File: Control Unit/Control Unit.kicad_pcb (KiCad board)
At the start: 2 copper layers, 100 x 76.5 mm, 17 parts, among them J1 PWR_IN, J2 LM2596S, J3 ST7789, J4 DHT20, J5 RTC, J6 RPM_IN, J7 Page flip, SW1 SW_DPST_x2, U1 ESP32-DEVKIT-V1, U2 PC817

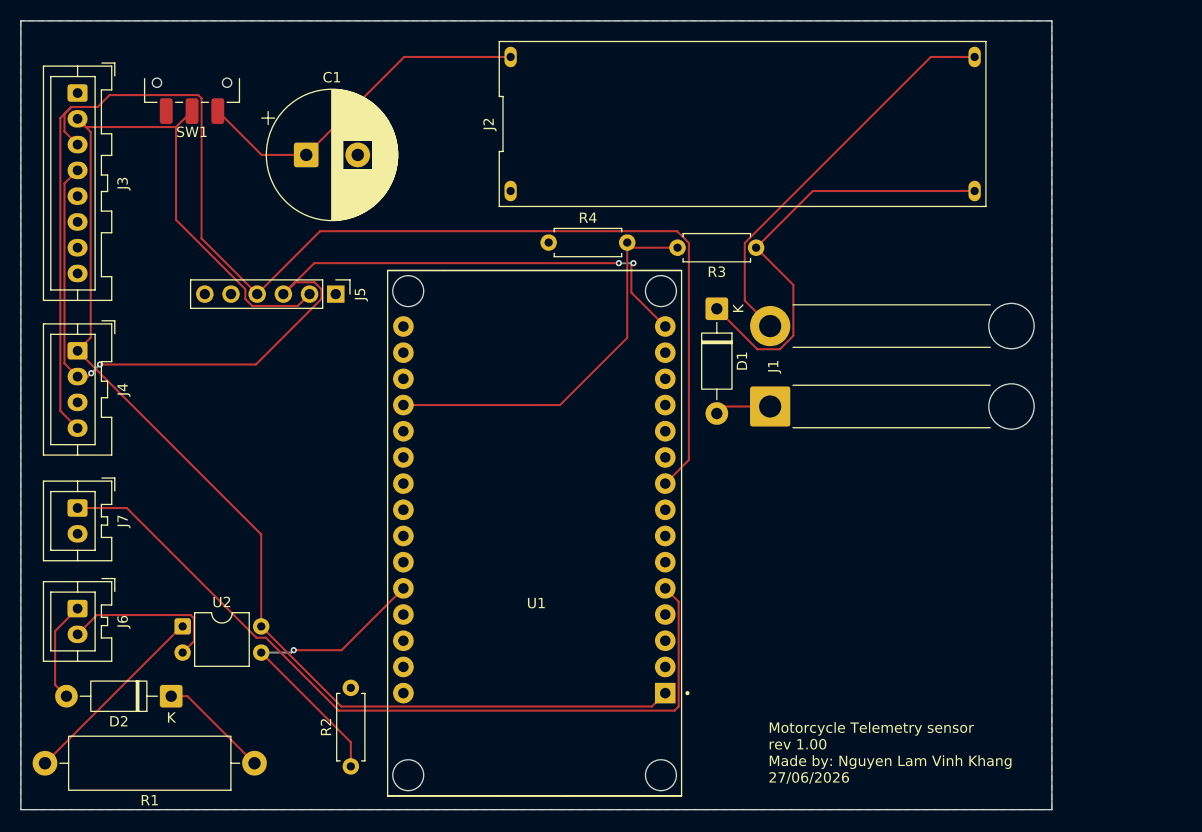
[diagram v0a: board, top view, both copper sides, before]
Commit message: rev 1.1: added relay to use power directly from battery
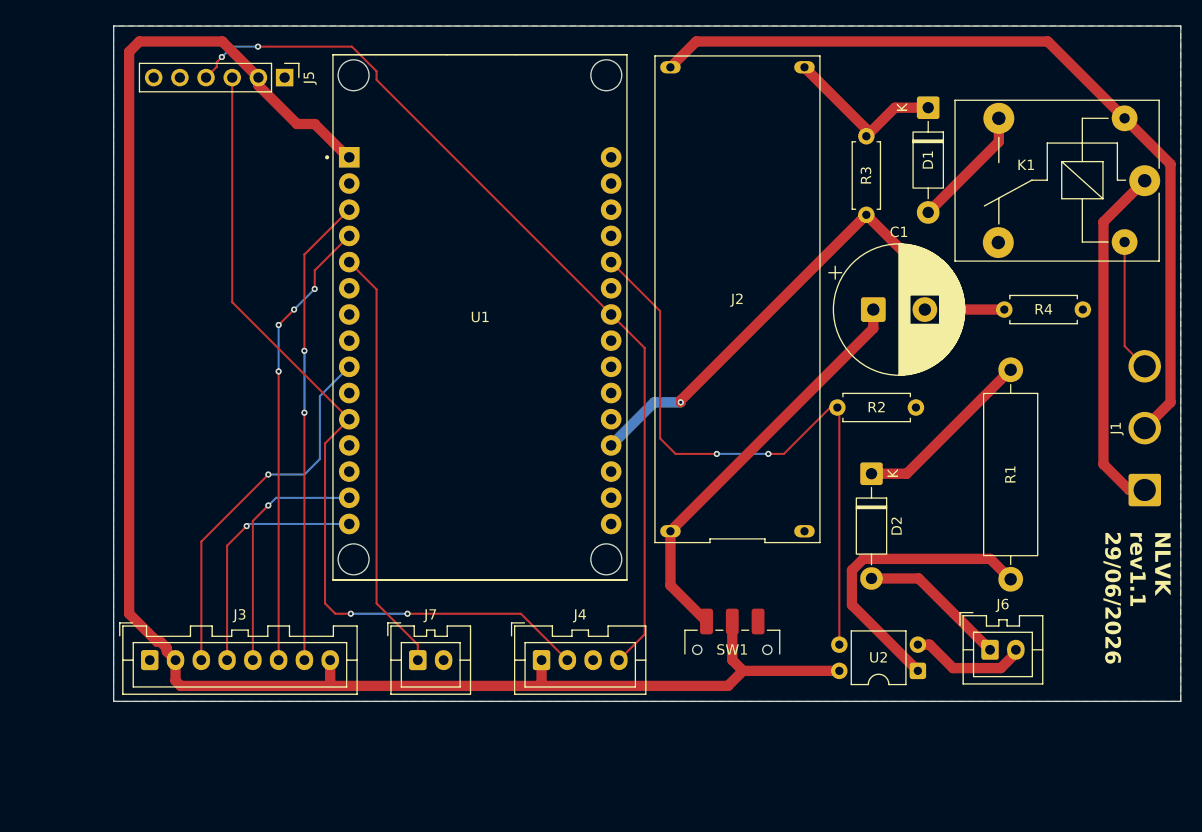
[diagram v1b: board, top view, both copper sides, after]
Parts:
- added K1: Relay_SPDT, Relay_THT:Relay_SPDT_SANYOU_SRD_Series_Form_C, F.Cu at (201.5, 95.0)
- J1: value PWR_IN -> Conn_01x03_Pin; footprint Connector_Wire:SolderWire-1.5sqmm_1x02_P7.8mm_D1.7mm_OD3.9mm_Relief -> Connector_Wire:SolderWire-1.5sqmm_1x03_P6mm_D1.7mm_OD3mm
- moved J6 88.6 mm to (186.5, 140.5), turned to 0 degrees
- moved R1 82.7 mm to (188.5, 113.3), turned to -90 degrees
- moved SW1 76.0 mm to (161.5, 140.5), turned to 0 degrees
- moved U2 71.4 mm to (179.5, 142.5), turned to 180 degrees
- moved D2 71.3 mm to (175.0, 123.4), turned to -90 degrees
- moved R2 58.6 mm to (171.7, 117.0), turned to 0 degrees
- moved C1 57.0 mm to (175.2, 107.5)
- moved J3 55.4 mm to (105.0, 141.5), turned to 0 degrees
- moved J4 54.1 mm to (143.0, 141.5), turned to 0 degrees
- moved R4 52.2 mm to (195.5, 107.5), turned to 180 degrees
- moved J1 37.2 mm to (201.5, 125.0)
- moved J7 36.1 mm to (131.0, 141.5), turned to 0 degrees
- moved D1 28.3 mm to (180.5, 87.9)
- moved U1 21.6 mm to (137.1, 108.2), turned to 0 degrees
- moved J5 21.6 mm to (118.1, 85.0)
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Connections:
- J1 pad 1: /12V_PWR_BATT -> /12V_PWR_Relay
- J3 pad 5: unconnected-(J3-RES-Pad5) -> Net-(J3-RES)
- J3 pad 6: unconnected-(J3-DC-Pad6) -> Net-(J3-DC)
- J3 pad 7: unconnected-(J3-CS-Pad7) -> Net-(J3-CS)
- J3 pad 8: unconnected-(J3-Pin_8-Pad8) -> /3.3V_PWR
- J4 pad 2: Net-(J3-SDA) -> Net-(J4-SDA)
- J4 pad 4: Net-(J3-SCL) -> Net-(J4-SCL)
- J5 pad 3: Net-(J3-SDA) -> Net-(J4-SDA)
- J5 pad 4: Net-(J3-SCL) -> Net-(J4-SCL)
- U1 pad 11: unconnected-(U1-D21-Pad11) -> Net-(J4-SDA)
- U1 pad 14: unconnected-(U1-D22-Pad14) -> Net-(J3-RES)
- U1 pad 24: unconnected-(U1-D26-Pad24) -> Net-(J4-SCL)
- U1 pad 3: unconnected-(U1-D15-Pad3) -> Net-(J3-CS)
- U1 pad 4: unconnected-(U1-D2-Pad4) -> Net-(J3-DC)
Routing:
- net Net-(J3-SCL): track 140.4 -> 36.4 mm, vias 0 -> 1
- net Net-(J4-SCL): track 0.00 -> 88.0 mm, vias 0 -> 2
- net Net-(J4-SDA): track 0.00 -> 82.5 mm, vias 0 -> 2
- net Net-(J3-SDA): track 96.0 -> 23.8 mm, vias 4 -> 1
- net Net-(J3-CS): track 0.00 -> 45.5 mm, vias 0 -> 2
- net Net-(J3-DC): track 0.00 -> 44.0 mm, vias 0 -> 4
- net /12V_GND: track 38.8 -> 81.1 mm
- net Net-(J7-SIG): track 78.6 -> 41.4 mm
- net /12V_PWR_Relay: track 0.00 -> 34.2 mm
- net Net-(U1-D14): track 31.0 -> 61.8 mm, vias 1 -> 2
- net /12V_PWR: track 43.1 -> 16.3 mm
- net /3.3V_PWR: track 139.1 -> 165.3 mm
- net Net-(J3-RES): track 0.00 -> 23.8 mm, vias 0 -> 1
- net Net-(J1-12V_SWITCH): track 0.00 -> 12.9 mm
- net Net-(U1-D34): track 38.7 -> 51.3 mm, vias 0 -> 1
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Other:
- board size 100 x 76.5 mm -> 103.5 x 65.5 mm
- board text added: "NLVK rev1.1 29/06/2026"
- board text removed: "Motorcycle Telemetry sensor rev 1.00 Made by: Nguyen Lam Vinh Khang 27/06/2026"

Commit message: rev 1.1b: optimized PCB size
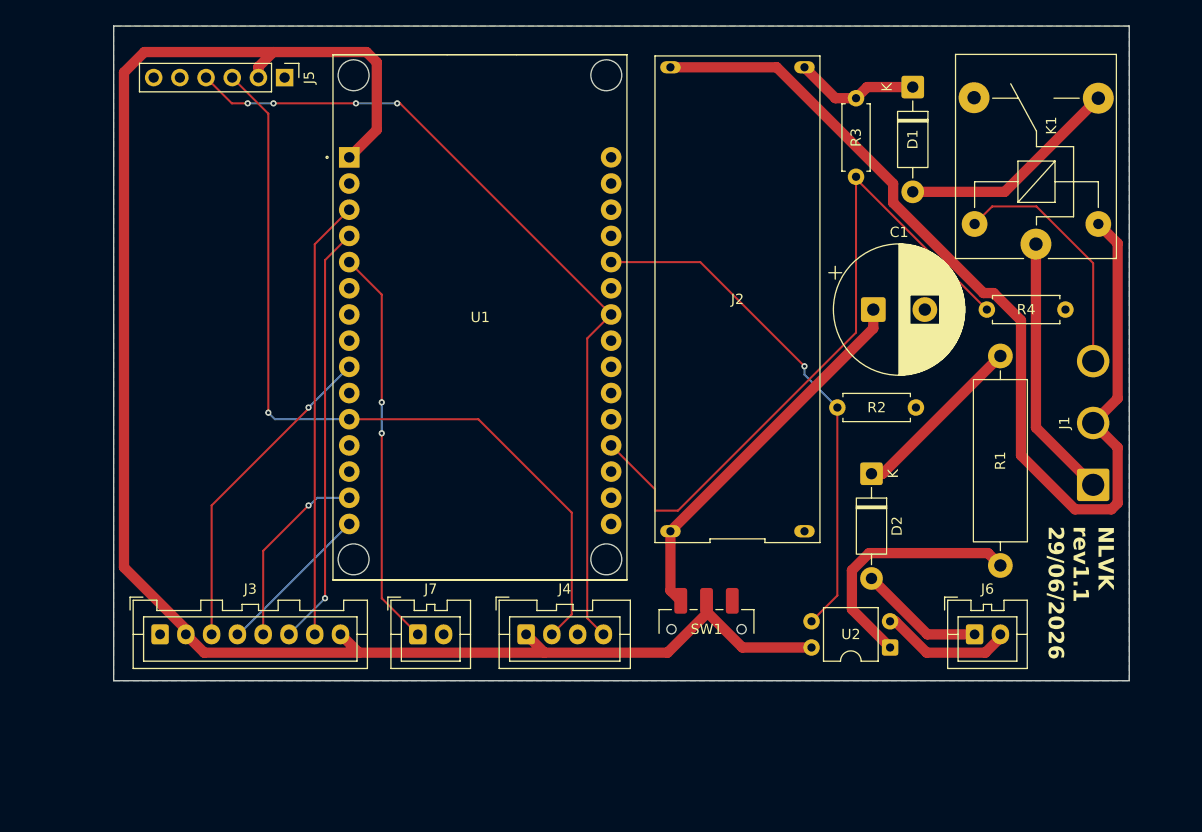
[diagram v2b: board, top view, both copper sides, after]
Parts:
- moved K1 12.2 mm to (190.9, 101.2), turned to 90 degrees
- moved J1 5.02 mm to (196.5, 124.5)
- moved R3 3.82 mm to (173.5, 87.0)
- moved U2 3.52 mm to (176.8, 140.3)
- moved SW1 3.20 mm to (159.0, 138.5)
- moved J4 2.92 mm to (141.5, 139.0)
- moved J3 2.69 mm to (106.0, 139.0)
- moved D1 2.50 mm to (179.0, 85.9)
- moved J7 2.50 mm to (131.0, 139.0)
- moved J6 2.12 mm to (185.0, 139.0)
- moved R4 1.69 mm to (193.8, 107.5)
- moved R1 1.67 mm to (187.5, 112.0)
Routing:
- net /12V_GND: track 81.1 -> 99.9 mm
- net Net-(U1-D34): track 51.3 -> 68.0 mm, vias 1 -> 0
- net Net-(U1-D14): track 61.8 -> 50.0 mm, vias 2 -> 1
- net Net-(J1-12V_SWITCH): track 12.9 -> 24.0 mm
- net /12V_PWR_BATT: track 12.0 -> 21.8 mm
- net /12V_PWR_Relay: track 34.2 -> 25.6 mm
- net Net-(J3-SDA): track 23.8 -> 15.3 mm, vias 1 -> 0
- net Net-(J4-SCL): track 88.0 -> 81.4 mm, vias 2 -> 4
- net Net-(J3-RES): track 23.8 -> 18.6 mm
- net Net-(J3-SCL): track 36.4 -> 31.5 mm
- net /RPM_PWR: track 29.1 -> 24.6 mm
- net /12V_PWR: track 16.3 -> 12.2 mm
- net /3.3V_PWR_SW: track 39.8 -> 36.8 mm
- net Net-(J3-DC): track 44.0 -> 41.1 mm, vias 4 -> 1
- net Net-(J3-CS): track 45.5 -> 42.6 mm, vias 2 -> 0
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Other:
- board size 103.5 x 65.5 mm -> 98.5 x 63.5 mm
